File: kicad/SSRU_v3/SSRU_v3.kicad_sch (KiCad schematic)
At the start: 99 parts, among them J1 AVR-ISP-6, J10 Conn_01x04, J11 Conn_01x02, J20 Conn_01x02, J21 Conn_01x02, J22 Conn_01x04, J23 Conn_01x02, J24 Conn_01x04, J25 Conn_01x02, J26 Conn_01x03, J27 Conn_01x03, J28 Conn_01x02, J29 Conn_01x02, J3 Conn_01x02, J30 Conn_01x02, SW1 SW_Push, U1 MCP2515-xSO, U10 TJA1051T, U11 Ai-Thinker-Ra-02, U12 TJA1051T, U2 ATmega328P-A, U3 TXS0102DCT, U4 LM2576S-5, U5 AMS1117-3.3, U7 MCP2515-xSO, U8 74LVC1G17, U9 MT3608/SDB628, Y1 16MHz, Y3 16MHz, Y4 16MHz

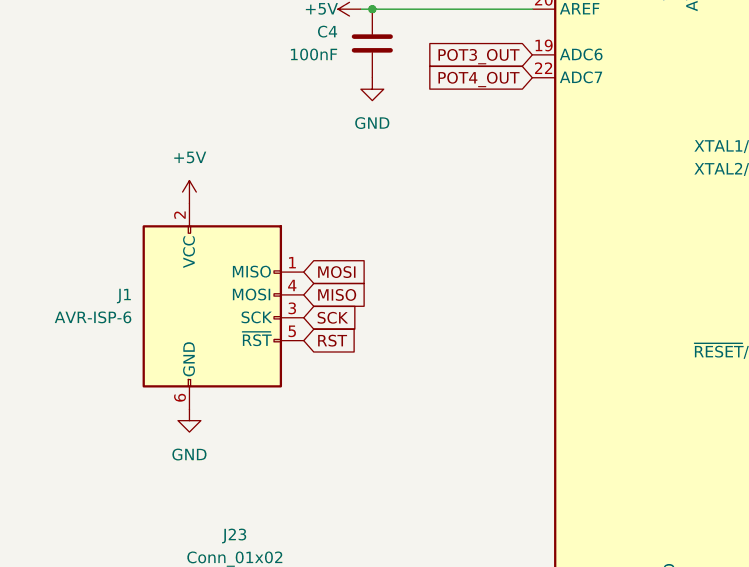
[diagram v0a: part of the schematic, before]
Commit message: ssru v3
current to voltage lm324 supply to  5v. icsp header mosi miso fixed
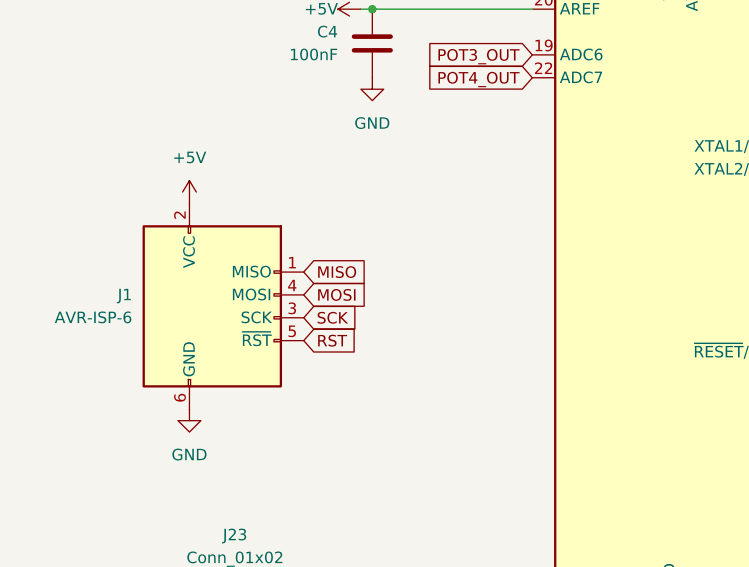
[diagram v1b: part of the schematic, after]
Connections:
- net MISO: now also J1.1 (MISO); no longer J1.4 (MOSI)
- net MOSI: now also J1.4 (MOSI); no longer J1.1 (MISO)
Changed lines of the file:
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@@
 	(global_label "MISO"
 		(shape input)
-		(at 36.83 66.04 0)
-		(fields_autoplaced yes)
-		(effects
-			(font
-				(size 1.27 1.27)
-			)
-			(justify left)
-		)
-		(property "Intersheetrefs" "${INTERSHEET_REFS}"
-			(at 44.4114 66.04 0)
+		(at 36.83 63.5 0)
+		(fields_autoplaced yes)
+		(effects
+			(font
+				(size 1.27 1.27)
+			)
+			(justify left)
+		)
+		(property "Intersheetrefs" "${INTERSHEET_REFS}"
+			(at 44.4114 63.5 0)
 			(effects
 				(font
@@
 	(global_label "MOSI"
 		(shape input)
-		(at 36.83 63.5 0)
-		(fields_autoplaced yes)
-		(effects
-			(font
-				(size 1.27 1.27)
-			)
-			(justify left)
-		)
-		(property "Intersheetrefs" "${INTERSHEET_REFS}"
-			(at 44.4114 63.5 0)
-			(effects
-				(font
+		(at 36.83 66.04 0)
+		(fields_autoplaced yes)
+		(effects
+			(font
+				(size 1.27 1.27)
+			)
+			(justify left)
+		)
+		(property "Intersheetrefs" "${INTERSHEET_REFS}"
+			(at 44.4114 66.04 0)
+			(effects
+				(font

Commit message: SSRU new layout
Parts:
- removed C37, C47: 100nF, RMC_Capacitor:C_0805_2012Metric_Pad1.18x1.45mm_HandSolder_L, symbol Device:C
- removed J28, J29: Conn_01x02, Connector_JST:JST_XH_B2B-XH-A_1x02_P2.50mm_Vertical, symbol Connector_Generic:Conn_01x02
- added C15, C16: 100nF, RMC_Capacitor:C_0805_2012Metric_Pad1.18x1.45mm_HandSolder_L, symbol Device:C
- added D6: SMA Diode, Diode_SMD:D_SMA_Handsoldering, symbol Device:D_Zener
- added F3: Fuse, to be sorted:Fuse_1210_3225Metric_Pad1.42x2.65mm_HandSolder, symbol Device:Fuse
- added J31: Conn_01x04, Connector_JST:JST_XH_B4B-XH-A_1x04_P2.50mm_Vertical, symbol Connector_Generic:Conn_01x04
- added U13: CH340N, Package_SO:SOP-8_3.9x4.9mm_P1.27mm, symbol Interface_USB:CH340N
- C11, C7: footprint Capacitor_THT:CP_Radial_D6.3mm_P2.50mm -> RMC_Capacitor:CP_Radial_D6.3mm_P2.50mm_handsolder
- C46: value 0.1uF -> 100nF
- F1, F2: footprint Fuse:Fuse_1210_3225Metric_Pad1.42x2.65mm_HandSolder -> to be sorted:Fuse_1210_3225Metric_Pad1.42x2.65mm_HandSolder
- U2: footprint Package_QFP:TQFP-32_7x7mm_P0.8mm -> RMC_QFP:TQFP-32_7x7mm_P0.8mm_L
- U3: footprint Package_SO:SSOP-8_2.95x2.8mm_P0.65mm -> RMC_SO:SOIC-8_3.9x4.9mm_P1.27mm_RMC_Handsolder
- U8: footprint Package_TO_SOT_SMD:SOT-23-5_HandSoldering -> RMC_SOT:SOT-23-5_HandSoldering_Extended_RMC
- U9: footprint Package_TO_SOT_SMD:SOT-23-6_Handsoldering -> RMC_SOT:SOT-23-6_Handsoldering_Extended_RMC
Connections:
- net POT3_IN is gone; now on net POT2_IN: U2.19 (ADC6)
- net POT4_IN is gone; now on net POT1_IN: U2.22 (ADC7)
- net +5V: now also C15.2, D6.1 (K), U13.5 (VCC)
- net CS_CAN1: now also U2.12 (PB0); no longer U2.13 (PB1)
- net CS_CAN2: now also U2.13 (PB1); no longer U2.14 (PB2)
- net CS_CAN3: now also U2.14 (PB2); no longer U2.30 (PD0)
- net GND: now also C15.1, C16.1, J31.1 (Pin_1), U13.3 (GND)
- net IRO: now also U2.24 (PC1); no longer U2.31 (PD1)
- net LVB_TEMP: now also U2.23 (PC0); no longer U2.12 (PB0)
- net POT1_IN: no longer U2.24 (PC1)
- net POT2_IN: no longer U2.23 (PC0)
- net PUMP_THERM_IN renamed PUMP_NTC_100k
- new net: F3.1, J31.4 (Pin_4)
- new net: D6.2 (A), F3.2
- new net: C16.2, U13.8 (V3)
- new net 328_RX: U13.6 (TXD), U2.30 (PD0)
- new net 328_TX: U13.7 (RXD), U2.31 (PD1)
- new net UD+: J31.2 (Pin_2), U13.1 (UD+)
- new net UD-: J31.3 (Pin_3), U13.2 (UD-)
- no-connect marks 19 -> 20

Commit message: SSRU new scheme
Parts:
- added J32: Conn_01x04, Connector_JST:JST_XH_B4B-XH-A_1x04_P2.50mm_Vertical, symbol Connector_Generic:Conn_01x04
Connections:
- net BRAKE_TEMP_OUT4 is gone; now on net FLOW_OUT: U2.9 (PD5)
- net +5V: now also J32.4 (Pin_4)
- net BRAKE_TEMP_OUT1: now also U2.23 (PC0); no longer U2.32 (PD2)
- net BRAKE_TEMP_OUT2: now also U2.24 (PC1); no longer U2.1 (PD3)
- net CS_CAN1: now also U1.16 (~{CS}); no longer U7.16 (~{CS})
- net CS_CAN2: now also U7.16 (~{CS}); no longer U1.16 (~{CS})
- net FLOW_OUT: no longer U2.11 (PD7)
- net GND: now also J32.1 (Pin_1)
- net IRO: now also U2.32 (PD2); no longer U2.24 (PC1)
- net LVB_S: now also U2.25 (PC2); no longer U2.10 (PD6)
- net LVB_TEMP: now also U2.11 (PD7); no longer U2.23 (PC0)
- net Temp_sensor: now also U2.10 (PD6); no longer U2.25 (PC2)
- net BRAKE_TEMP_OUT3 renamed ENCODER_B
- net ENCODER_B: now also J32.3 (Pin_3)
- new net ENCODER_A: J32.2 (Pin_2), U2.1 (PD3)
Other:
- note added: "MCU CAN"
- note added: "SSRU CAN"
- note removed: "BMS"
- note removed: "DATA LOGGER"
- moved on the sheet: C26, C27, C31, C39, C40, C41, C42, C43, C44, C45, C46, J25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

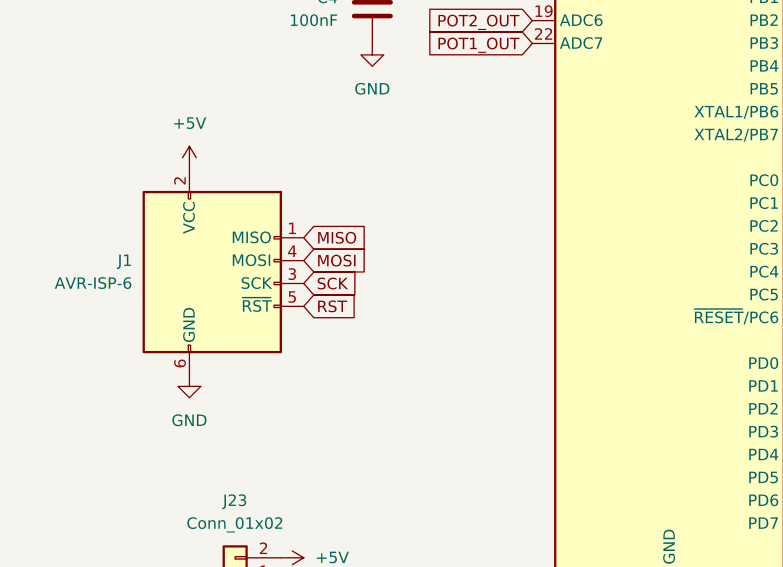
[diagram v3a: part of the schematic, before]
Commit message: created TS schematics
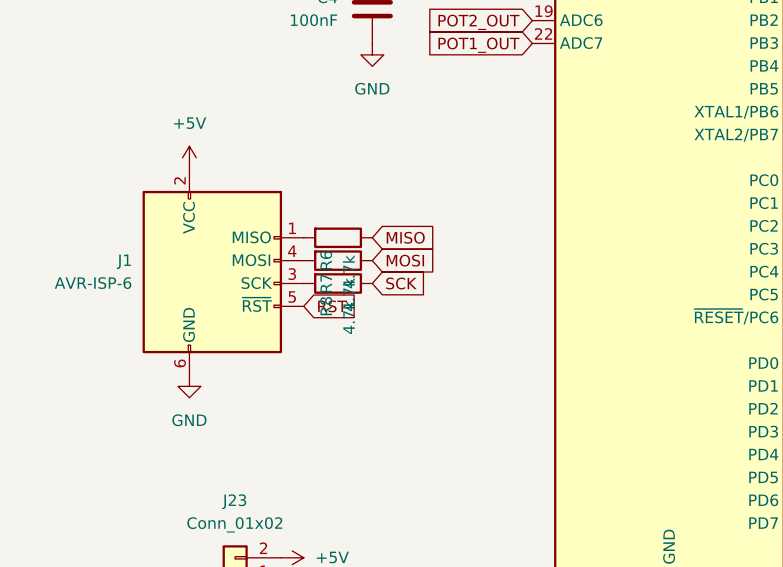
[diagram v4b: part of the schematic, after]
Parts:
- added R6, R7, R8: 4.7k, RMC_Resistor:R_0805_2012Metric_Pad1.20x1.40mm_HandSolder_L, symbol Device:R
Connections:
- net MISO: now also R6.1; no longer J1.1 (MISO)
- net MOSI: now also R7.1; no longer J1.4 (MOSI)
- net SCK: now also R8.1; no longer J1.3 (SCK)
- new net: J1.1 (MISO), R6.2
- new net: J1.3 (SCK), R8.2
- new net: J1.4 (MOSI), R7.2

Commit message: SSRU V3
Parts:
- removed J10: Conn_01x04, Connector_JST:JST_XH_B4B-XH-A_1x04_P2.50mm_Vertical, symbol Connector_Generic:Conn_01x04
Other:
- sheet current to voltage ports: added none; removed BRAKE_TEMP_OUT3, BRAKE_TEMP_OUT4
